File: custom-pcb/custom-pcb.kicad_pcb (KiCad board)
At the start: 2 copper layers, 72.4 x 72.4 mm, 68 parts, among them J1 CONN_CTL, J2 CONN_UART, J3 CONN_DBRD_IN, J4 CONN_DBRD_OUT, SW1 RESET, SW10 RESET_D, SW11 BOOT_D, SW2 BOOT, SW3 SPR_POWER, SW4 SPR_FAN, SW5 SPR_NIGHT, SW6 SPR_TIMER, SW7 SPR_FILTER, SW8 SPR_LIGHT, SW9 SPR_LOCK, U1 AMS1117-3.3, U2 74HCT595PW,118, U3 74HCT595PW,118, U4 ESP32-WROOM-32

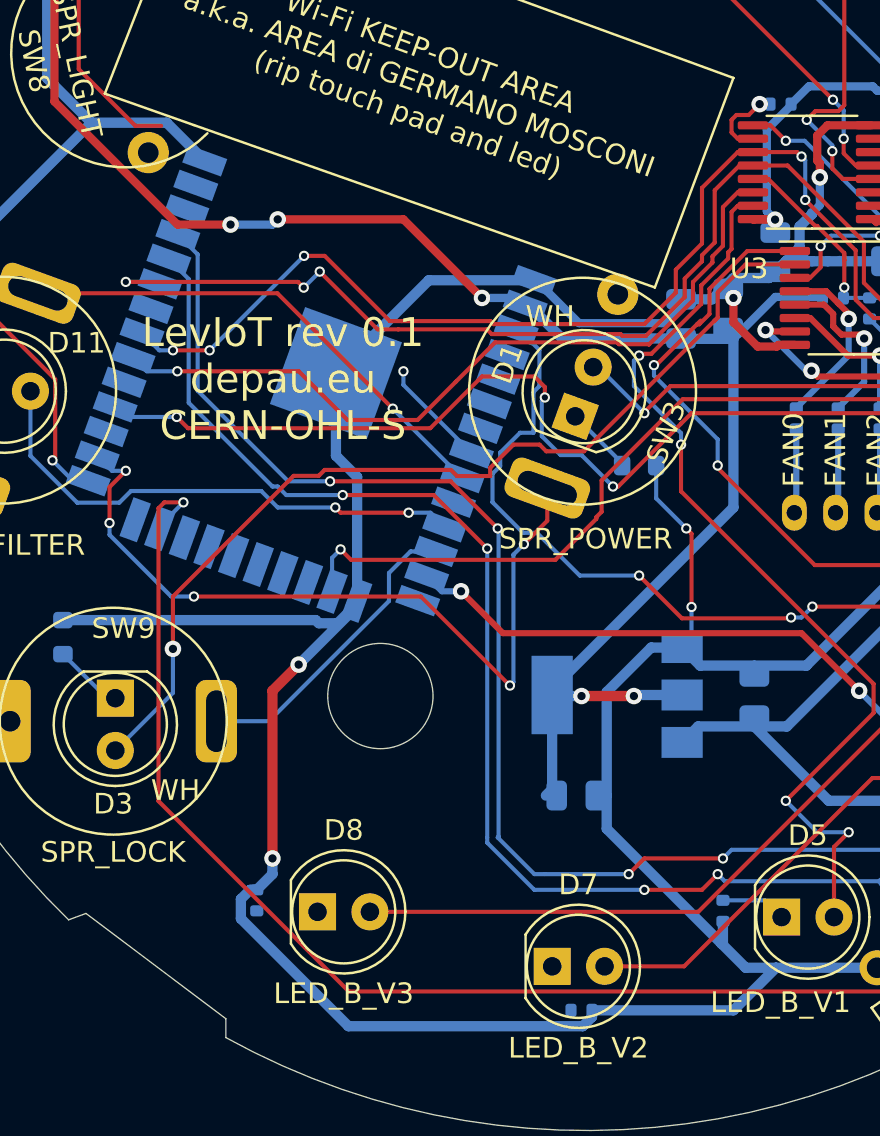
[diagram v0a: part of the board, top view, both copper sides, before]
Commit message: Connect unconnected pads
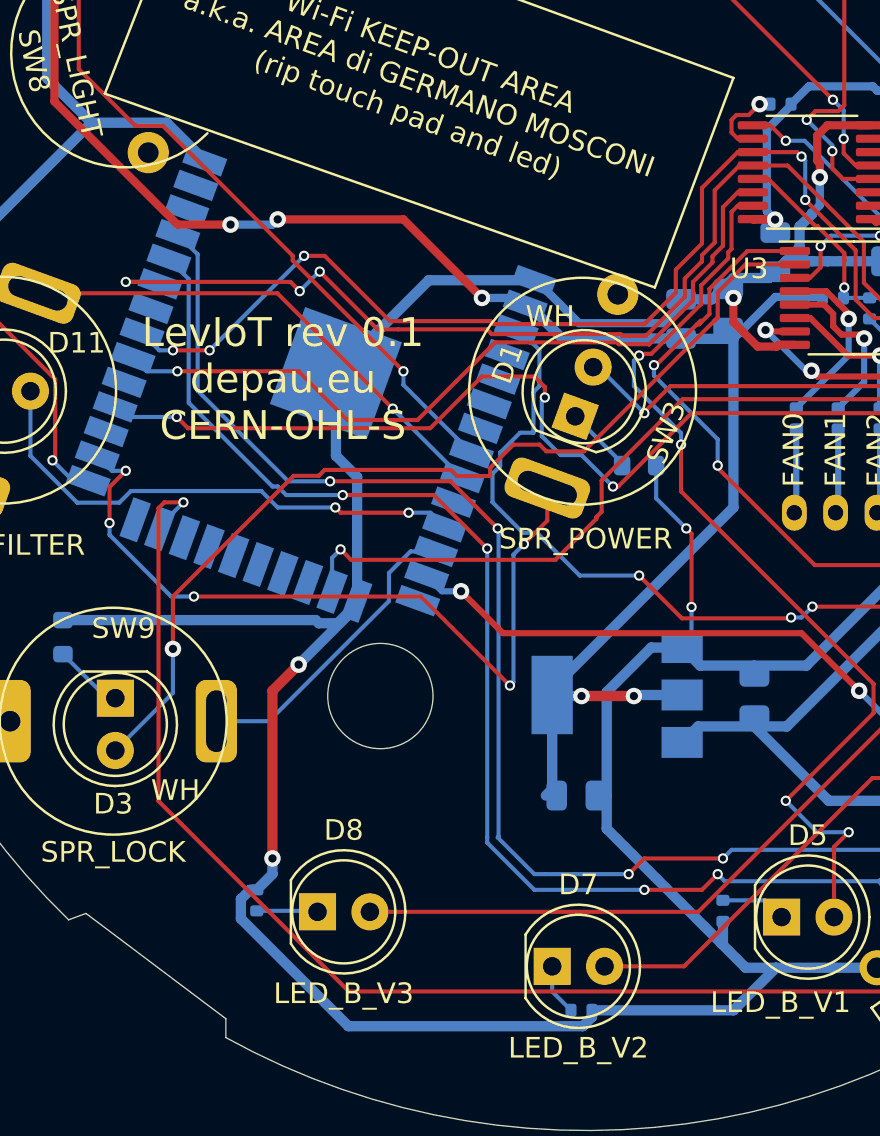
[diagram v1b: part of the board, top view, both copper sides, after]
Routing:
- net TOUCH_LIGHT: track 16.7 -> 33.5 mm
- net Net-(D8-Pad1): track 0.00 -> 2.97 mm
- net Net-(D7-Pad1): track 0.00 -> 2.51 mm
- net GND: track 364.7 -> 365.7 mm
- net +3V3: track 138.3 -> 138.9 mm
- net VCC: track 77.7 -> 78.3 mm

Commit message: Latest changes
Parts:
- added ?: , custom-pcb:OSHW-LOGO-L, F.Cu at (99.6, 81.5)
- added C10: 0u1, Capacitor_SMD:C_0402_1005Metric, B.Cu at (142.9, 73.2)
- added C11: 0u1, Capacitor_SMD:C_0402_1005Metric, B.Cu at (100.1, 98.6)
- added C12: 0u1, Capacitor_SMD:C_0402_1005Metric, B.Cu at (136.2, 73.9)
- added C13: 0u1, Capacitor_SMD:C_0402_1005Metric, B.Cu at (125.8, 105.6)
- added C14: 0u1, Capacitor_SMD:C_0402_1005Metric, B.Cu at (125.0, 56.9)
- added C15: 0u1, Capacitor_SMD:C_0402_1005Metric, B.Cu at (114.8, 107.7)
- added C16: 0u1, Capacitor_SMD:C_0402_1005Metric, B.Cu at (96.8, 57.4)
- added C17: 0u1, Capacitor_SMD:C_0402_1005Metric, B.Cu at (101.1, 105.5)
- added C18: 0u1, Capacitor_SMD:C_0402_1005Metric, B.Cu at (128.1, 94.8)
- added C19: 0u1, Capacitor_SMD:C_0402_1005Metric, B.Cu at (128.9, 56.0)
- added C20: 0u1, Capacitor_SMD:C_0402_1005Metric, B.Cu at (125.0, 55.9)
- added C21: 0u1, Capacitor_SMD:C_0402_1005Metric, B.Cu at (85.2, 72.8)
- added C9: 0u1, Capacitor_SMD:C_0402_1005Metric, B.Cu at (121.8, 82.9)
- added R28: 510R, Resistor_SMD:R_0402_1005Metric, B.Cu at (117.6, 73.9)
- added R29: 510R, Resistor_SMD:R_0402_1005Metric, B.Cu at (133.6, 90.8)
- added R30: 510R, Resistor_SMD:R_0402_1005Metric, B.Cu at (135.3, 78.0)
- added R31: 510R, Resistor_SMD:R_0402_1005Metric, B.Cu at (129.3, 65.4)
- added R32: 510R, Resistor_SMD:R_0402_1005Metric, B.Cu at (92.5, 77.5)
- added R33: 510R, Resistor_SMD:R_0402_1005Metric, B.Cu at (94.2, 71.8)
- added R34: 510R, Resistor_SMD:R_0402_1005Metric, B.Cu at (95.0, 91.1)
- added REF**: ToolingHole_1.152mm_(for_JLCPCB_SMT), custom-pcb:ToolingHole_1.152mm_(for_JLCPCB_SMT), F.Cu at (128.0, 50.4)
- added REF**: ToolingHole_1.152mm_(for_JLCPCB_SMT), custom-pcb:ToolingHole_1.152mm_(for_JLCPCB_SMT), F.Cu at (98.9, 110.1)
- C5: value 0u1 -> 10u
- D1: value LED_W_POWER -> On/Off; footprint LED_THT:LED_D5.0mm -> custom-pcb:LED_D5.0mm-centered
- D10: value LED_B_2H -> 2H; footprint LED_THT:LED_D5.0mm -> LED_SMD:LED_0603_1608Metric_Pad1.05x0.95mm_HandSolder
- D11, D13, D2, D3, D4: footprint LED_THT:LED_D5.0mm -> custom-pcb:LED_D5.0mm-centered
- D12: value LED_B_4H -> 4H; footprint LED_THT:LED_D5.0mm -> LED_SMD:LED_0603_1608Metric_Pad1.05x0.95mm_HandSolder
- D5: value LED_B_V1 -> I; footprint LED_THT:LED_D5.0mm -> LED_SMD:LED_0603_1608Metric_Pad1.05x0.95mm_HandSolder
- D6: value LED_B_6H -> 6H; footprint LED_THT:LED_D5.0mm -> LED_SMD:LED_0603_1608Metric_Pad1.05x0.95mm_HandSolder
- D7: value LED_B_V2 -> II; footprint LED_THT:LED_D5.0mm -> LED_SMD:LED_0603_1608Metric_Pad1.05x0.95mm_HandSolder
- D8: value LED_B_V3 -> III; footprint LED_THT:LED_D5.0mm -> LED_SMD:LED_0603_1608Metric_Pad1.05x0.95mm_HandSolder
- D9: value LED_B_8H -> 8H; footprint LED_THT:LED_D5.0mm -> LED_SMD:LED_0603_1608Metric_Pad1.05x0.95mm_HandSolder
- J2: footprint Connector_PinHeader_2.54mm:PinHeader_1x04_P2.54mm_Horizontal -> Connector_PinHeader_2.54mm:PinHeader_1x04_P2.54mm_Vertical
- J4: footprint Connector_PinHeader_2.54mm:PinHeader_1x03_P2.54mm_Horizontal -> Connector_PinHeader_2.54mm:PinHeader_1x03_P2.54mm_Vertical
- SW4: value SPR_FAN -> Fan speed
- SW5: value SPR_NIGHT -> Night mode
- SW6: value SPR_TIMER -> Timer
- SW7: value SPR_FILTER -> Filter
- SW8: value SPR_LIGHT -> Light; footprint touchpad_spring:touchpad_sprint_nosilk -> touchpad_spring:touchpad_spring
- SW9: value SPR_LOCK -> Lock
- U2, U3: moved to B.Cu
- moved SW2 63.9 mm to (128.3, 111.0), turned to -60 degrees
- moved SW1 51.4 mm to (132.7, 108.3), turned to -55 degrees
- moved J4 48.9 mm to (122.8, 114.0), turned to -79 degrees
- moved R25 29.7 mm to (99.3, 68.8), turned to -90 degrees
- moved C6 26.6 mm to (100.5, 74.0), turned to 100 degrees
- moved C8 26.2 mm to (122.7, 52.1), turned to 100 degrees
- moved R15 26.1 mm to (99.4, 74.2), turned to -80 degrees
- moved J2 25.9 mm to (110.4, 114.9), turned to -103 degrees
- moved C7 25.9 mm to (124.7, 51.8), turned to 100 degrees
- moved R21 25.8 mm to (101.4, 73.9), turned to 100 degrees
- moved R23 22.6 mm to (108.7, 109.0), turned to 77 degrees
- moved R24 21.3 mm to (107.7, 108.7), turned to 77 degrees
- moved U4 21.2 mm to (110.6, 62.2), turned to -170 degrees
- moved C4 19.8 mm to (103.1, 84.3)
- moved R2 16.5 mm to (120.1, 88.0), turned to 180 degrees
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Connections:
- SW3 pad 1: TOUCH_POWER -> Net-(R28-Pad1)
- SW4 pad 1: TOUCH_FAN -> Net-(R29-Pad1)
- SW5 pad 1: TOUCH_NIGHT -> Net-(R30-Pad1)
- SW6 pad 1: TOUCH_TIMER -> Net-(R31-Pad1)
- SW7 pad 1: TOUCH_FILTER -> Net-(R32-Pad1)
- SW8 pad 1: TOUCH_LIGHT -> Net-(R33-Pad1)
- SW9 pad 1: TOUCH_LOCK -> Net-(R34-Pad1)
- U4 pad 12: TOUCH_LOCK -> TOUCH_TIMER
- U4 pad 14: (no net) -> TOUCH_POWER
- U4 pad 16: TOUCH_NIGHT -> TOUCH_LOCK
- U4 pad 23: TOUCH_TIMER -> (no net)
- U4 pad 26: TOUCH_POWER -> TOUCH_FILTER
- U4 pad 9: TOUCH_FILTER -> TOUCH_NIGHT
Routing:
- net GND: track 365.7 -> 226.0 mm, vias 10 -> 34
- net TOUCH_TIMER: track 122.8 -> 9.43 mm, vias 1 -> 0
- net Net-(R17-Pad1): track 90.7 -> 13.7 mm, vias 6 -> 0
- net EN: track 26.2 -> 89.3 mm, vias 1 -> 0
- net Net-(R21-Pad2): track 54.8 -> 3.07 mm, vias 2 -> 0
- net Net-(R25-Pad1): track 53.2 -> 3.82 mm, vias 4 -> 0
- net LED_RED_FILTER: track 25.1 -> 62.1 mm
- net SHIFT_OUTEN: track 11.9 -> 47.3 mm, vias 2 -> 4
- net TOUCH_POWER: track 37.9 -> 6.35 mm, vias 5 -> 0
- net IO0: track 50.0 -> 74.6 mm, vias 1 -> 6
- net TOUCH_LOCK: track 14.8 -> 33.0 mm
- net TOUCH_NIGHT: track 41.9 -> 24.6 mm, vias 1 -> 2
- net TOUCH_LIGHT: track 33.5 -> 48.5 mm, vias 1 -> 8
- net LED_BLUE_6H: track 25.3 -> 39.4 mm, vias 2 -> 3
- net LED_WHITE_FAN: track 44.8 -> 31.3 mm, vias 1 -> 2
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- added copper zone on B.Cu, net GND
- added copper zone on F.Cu, net GND
- added copper zone on In2.Cu, net GND
- added copper zone on B.Cu, net GND1
- added copper zone on F.Cu, net GND1
- added copper zone on In2.Cu, net GND1
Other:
- board size 72.4 x 72.4 mm -> 72.4 x 72.3 mm
- copper layers 2 -> 4
- net class Default removed
- board text added: "+"
- board text added: "DBOARD"
- board text added: "LevIoT rev 0.2 depau.eu CERN-OHL-S"
- board text added: "¯\_(ツ)_/¯"
- board text removed: "BUTTONS DBRD"
- board text removed: "LED 2H"
- board text removed: "LED 4H"
- board text removed: "LED 6H"
- board text removed: "LED 8H"
- board text removed: "LED V1"
- board text removed: "LED V2"
- board text removed: "LED V3"
- board text removed: "LevIoT rev 0.1 depau.eu CERN-OHL-S"
- board text removed: "Wi-Fi KEEP-OUT AREA a.k.a. AREA di GERMANO MOSCONI"
- board text removed: "Wi-Fi KEEP-OUT AREA a.k.a. AREA di GERMANO MOSCONI (rip touch pad and led)"
